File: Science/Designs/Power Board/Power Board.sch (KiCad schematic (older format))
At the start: 13 parts

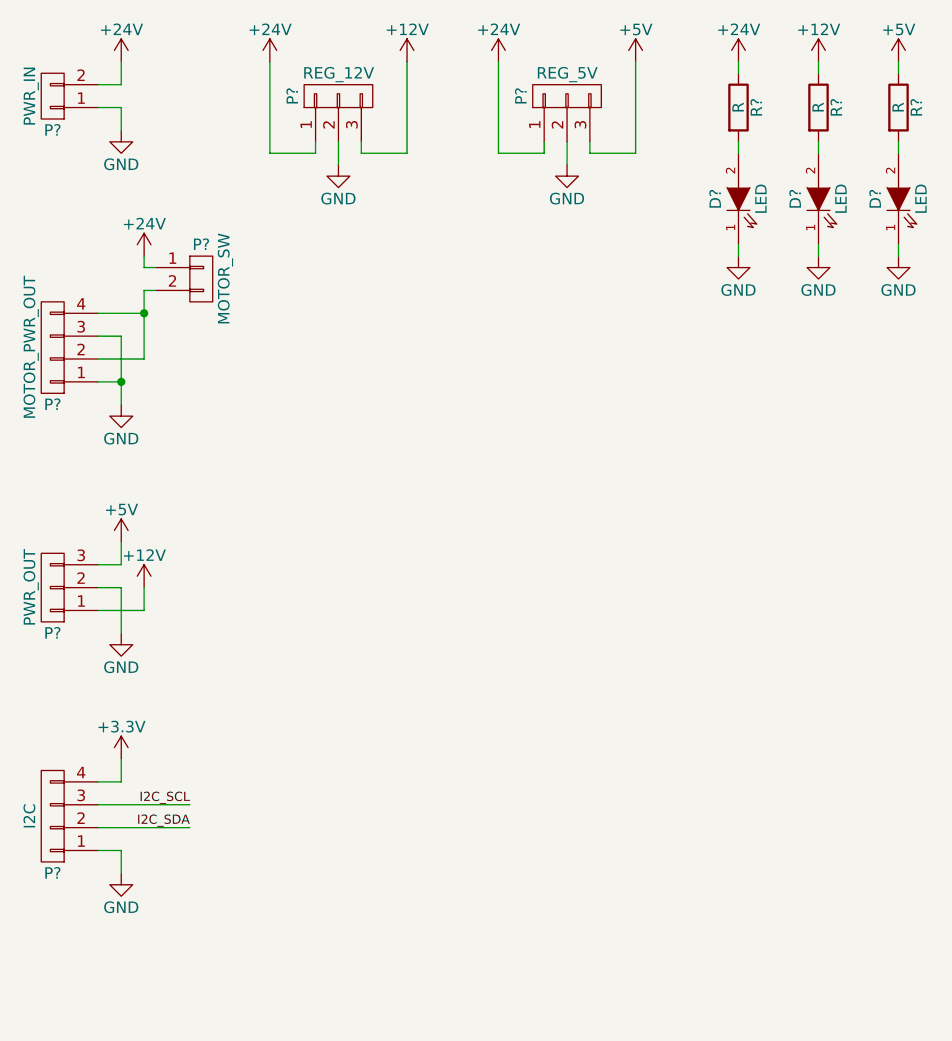
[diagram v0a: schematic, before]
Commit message: Current sensing on power board
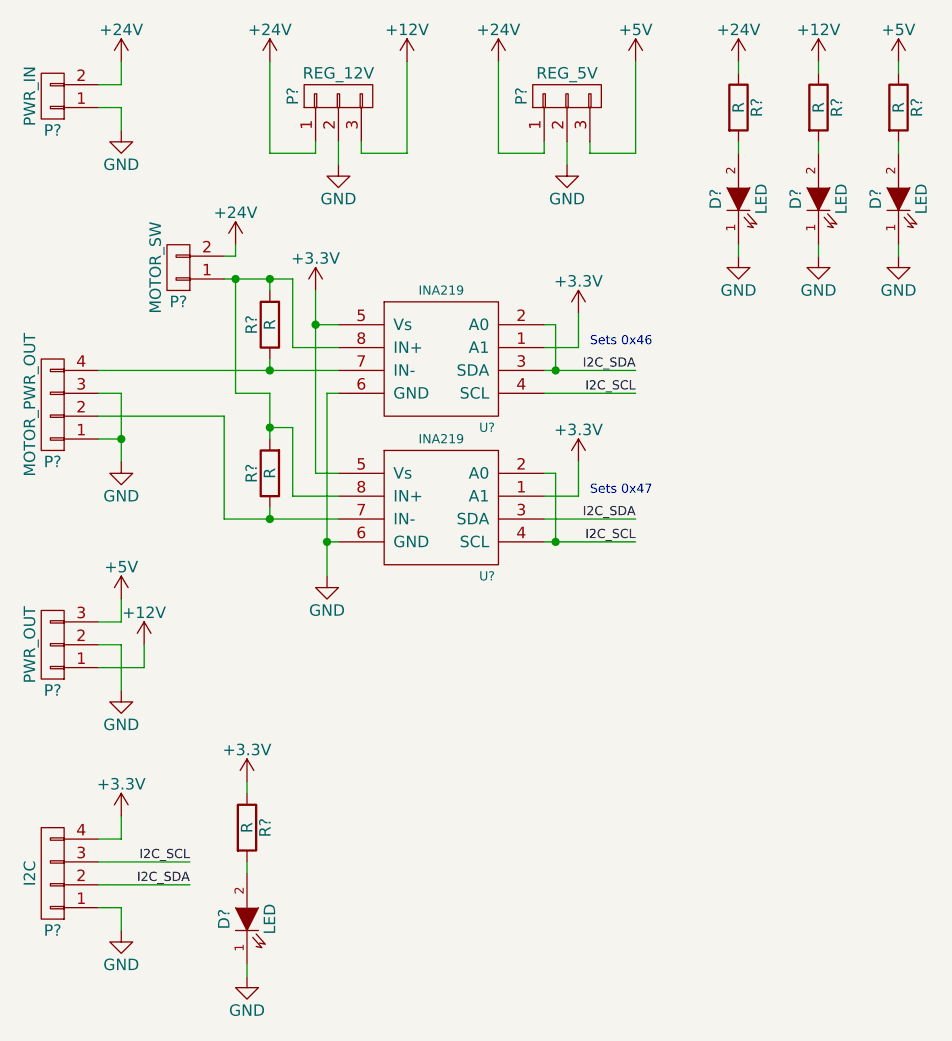
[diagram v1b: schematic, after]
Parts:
- added D?: LED, symbol LED
- added R? (x3): R, symbol R
- added U? (x2): INA219, symbol INA219
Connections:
- net +24V: now also P?.2 (P2); no longer P?.1 (P1)
- net +3V3: now also R?.1, U?.1 (A1), U?.1 (A1), U?.5 (Vs), U?.5 (Vs)
- net +5V: now also R?.1; no longer R?.1
- net GND: now also D?.1 (K), U?.6 (GND), U?.6 (GND)
- net I2C_SCL: now also U?.2 (A0), U?.4 (SCL), U?.4 (SCL)
- net I2C_SDA: now also U?.2 (A0), U?.3 (SDA), U?.3 (SDA)
- new net: P?.2 (P2), R?.1, U?.7 (IN-)
- new net: P?.4 (P4), R?.1, U?.7 (IN-)
- new net: P?.1 (P1), R?.2, R?.2, U?.8 (IN+), U?.8 (IN+)
- new net: D?.2 (A), R?.2
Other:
- note added: "Sets 0x46"
- note added: "Sets 0x47"
- moved on the sheet: D?, P?, R?

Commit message: Adding component values, system current sensor
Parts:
- added C? (x3): 100nF, symbol C
- added R?: 150mΩ, symbol R
- added R?: 2mΩ, symbol R
- added U?: INA219, symbol INA219
- R?: value R -> 1.5kΩ
- R?: value R -> 820Ω
- R?: value R -> 120Ω
- R?: value R -> 2mΩ
- R?: value R -> 10mΩ
- R?: value R -> 220Ω
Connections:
- net +24V: now also R?.1, U?.7 (IN-); no longer P?.2 (P2), P?.2 (P2)
- net +3V3: now also C?.1, C?.1, C?.1, U?.5 (Vs)
- net GND: now also C?.2, C?.2, C?.2, U?.2 (A0), U?.6 (GND)
- net I2C_SCL: now also U?.4 (SCL)
- net I2C_SDA: now also U?.1 (A1), U?.3 (SDA)
- net at P?.4 (P4), R?.1, U?.7 (IN-): now also R?.1
- net at P?.1 (P1), R?.2, R?.2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: now also R?.2
- new net 24V_IN: P?.2 (P2), P?.2 (P2), R?.2, U?.8 (IN+)
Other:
- note added: "Sets 0x48"
- moved on the sheet: P?

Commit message: Fixed issues
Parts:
- removed U? (x3): INA219, symbol INA219
- added U? (x3): INA219, symbol INA219
- P?: value PWR_OUT -> MAIN_PWR_OUT
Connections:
- net +24V: now also U?.7 (IN-)
- net +3V3: now also U?.1 (A1), U?.1 (A1), U?.5 (Vs), U?.5 (Vs), U?.5 (Vs)
- net 24V_IN: now also U?.8 (IN+)
- net GND: now also U?.2 (A0), U?.6 (GND), U?.6 (GND), U?.6 (GND)
- net I2C_SCL: now also U?.2 (A0), U?.4 (SCL), U?.4 (SCL), U?.4 (SCL)
- net I2C_SDA: now also U?.1 (A1), U?.2 (A0), U?.3 (SDA), U?.3 (SDA), U?.3 (SDA)
- net at P?.2 (P2), R?.1: now also U?.7 (IN-)
- net at P?.4 (P4), R?.1, R?.1: now also U?.7 (IN-)
- net at P?.1 (P1), R?.2, R?.2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: now also U?.8 (IN+), U?.8 (IN+)
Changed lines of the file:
@@
 P 1500 3500
 F 0 "P?" H 1500 3700 50  0000 C CNN
-F 1 "PWR_OUT" V 1600 3500 50  0000 C CNN
+F 1 "MAIN_PWR_OUT" V 1600 3500 50  0000 C CNN
 F 2 "" H 1500 3500 50  0000 C CNN
 F 3 "" H 1500 3500 50  0000 C CNN
@@
 	1    1850 1850
 	-1   0    0    1
-$EndComp
-$Comp
-L INA219 U?
-U 1 1 5A23D83B
-P 3200 2250
-F 0 "U?" H 3400 1950 40  0000 C CNN
-F 1 "INA219" H 3200 2550 40  0000 C CNN
-F 2 "" H 3200 2250 40  0001 C CNN
-F 3 "" H 3200 2250 40  0001 C CNN
-	1    3200 2250
-	1    0    0    -1
-$EndComp
-$Comp
-L INA219 U?
-U 1 1 5A23D894
-P 3200 2900
-F 0 "U?" H 3400 2600 40  0000 C CNN
-F 1 "INA219" H 3200 3200 40  0000 C CNN
-F 2 "" H 3200 2900 40  0001 C CNN
-F 3 "" H 3200 2900 40  0001 C CNN
-	1    3200 2900
-	1    0    0    -1
 $EndComp
 $Comp
@@
 Text Notes 3850 2850 0    40   ~ 0
 Sets 0x47
-$Comp
-L INA219 U?
-U 1 1 5A516F51
-P 3700 4000
-F 0 "U?" H 3900 3700 40  0000 C CNN
-F 1 "INA219" H 3700 4300 40  0000 C CNN
-F 2 "" H 3700 4000 40  0001 C CNN
-F 3 "" H 3700 4000 40  0001 C CNN
-	1    3700 4000
-	1    0    0    -1
-$EndComp
 Text Label 4550 4050 2    40   ~ 0
 I2C_SDA
@@
 	2250 2250 2250 2300
 Connection ~ 2250 2300
+$Comp
+L INA219 U?
+U 1 1 5A5E4452
+P 3200 2250
+F 0 "U?" H 3400 1950 40  0000 C CNN
+F 1 "INA219" H 3200 2550 40  0000 C CNN
+F 2 "" H 3200 2250 40  0001 C CNN
+F 3 "" H 3200 2250 40  0001 C CNN
+	1    3200 2250
+	1    0    0    -1
+$EndComp
+$Comp
+L INA219 U?
+U 1 1 5A5E4536
+P 3200 2900
+F 0 "U?" H 3400 2600 40  0000 C CNN
+F 1 "INA219" H 3200 3200 40  0000 C CNN
+F 2 "" H 3200 2900 40  0001 C CNN
+F 3 "" H 3200 2900 40  0001 C CNN
+	1    3200 2900
+	1    0    0    -1
+$EndComp
+$Comp
+L INA219 U?
+U 1 1 5A5E4596
+P 3700 4000
+F 0 "U?" H 3900 3700 40  0000 C CNN
+F 1 "INA219" H 3700 4300 40  0000 C CNN
+F 2 "" H 3700 4000 40  0001 C CNN
+F 3 "" H 3700 4000 40  0001 C CNN
+	1    3700 4000
+	1    0    0    -1
+$EndComp
 $EndSCHEMATC

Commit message: Began Power Board layout
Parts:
- D? (x4): symbol LED -> LED-RESCUE-Power_Board
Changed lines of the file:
@@
 EESchema Schematic File Version 2
+LIBS:Power Board-rescue
 LIBS:power
 LIBS:device
@@
 $EndComp
 Wire Wire Line
-	1700 2300 2250 2300
-Wire Wire Line
-	2250 2300 2450 2300
-Wire Wire Line
-	2450 2300 2750 2300
+	1700 2300 2750 2300
 Wire Wire Line
 	1700 2500 2250 2500
@@
 	1700 2400 1800 2400
 Wire Wire Line
-	1800 2400 1800 2600
-Wire Wire Line
-	1800 2600 1800 2700
+	1800 2400 1800 2700
 Wire Wire Line
 	1700 2600 1800 2600
@@
 $EndComp
 $Comp
-L LED D?
+L LED-RESCUE-Power_Board D?
 U 1 1 5A235063
 P 4500 1550
@@
 $EndComp
 $Comp
-L LED D?
+L LED-RESCUE-Power_Board D?
 U 1 1 5A235495
 P 4850 1550
@@
 $EndComp
 $Comp
-L LED D?
+L LED-RESCUE-Power_Board D?
 U 1 1 5A235672
 P 2350 4700
@@
 Connection ~ 2450 2300
 Wire Wire Line
-	2250 2950 2450 2950
-Wire Wire Line
-	2450 2950 2750 2950
+	2250 2950 2750 2950
 Wire Wire Line
 	2450 2950 2450 2900
@@
 Connection ~ 2450 2950
 Wire Wire Line
-	2450 2400 2450 2550
-Wire Wire Line
-	2450 2550 2450 2600
+	2450 2400 2450 2600
 Wire Wire Line
 	2450 2550 2550 2550
@@
 Connection ~ 2100 1900
 Wire Wire Line
-	2050 1900 2100 1900
-Wire Wire Line
-	2100 1900 2250 1900
-Wire Wire Line
-	2250 1900 2450 1900
-Wire Wire Line
-	2450 1900 2550 1900
+	2050 1900 2550 1900
 Wire Wire Line
 	2050 1800 2350 1800
 Wire Wire Line
-	2650 1950 2650 2100
-Wire Wire Line
-	2650 2100 2650 2750
+	2650 1950 2650 2750
 Connection ~ 2650 2100
 Wire Wire Line
 	2750 2400 2700 2400
 Wire Wire Line
-	2700 2400 2700 3050
-Wire Wire Line
-	2700 3050 2700 3200
+	2700 2400 2700 3200
 Wire Wire Line
 	2700 3050 2750 3050
@@
 I2C_SCL
 Wire Wire Line
-	3650 3050 3700 3050
-Wire Wire Line
-	3700 3050 4050 3050
+	3650 3050 4050 3050
 Wire Wire Line
 	3650 2950 4050 2950
@@
 	3650 2400 4050 2400
 Wire Wire Line
-	3650 2300 3700 2300
-Wire Wire Line
-	3700 2300 4050 2300
+	3650 2300 4050 2300
 $Comp
 L +3.3V #PWR?
@@
 $EndComp
 $Comp
-L LED D?
+L LED-RESCUE-Power_Board D?
 U 1 1 5A2432EE
 P 5200 1550
@@
 P 3000 3850
 F 0 "R?" V 3080 3850 50  0000 C CNN
-F 1 "150mΩ" V 3000 3850 50  0000 C CNN
+F 1 "150mΩ" V 3000 3850 39  0000 C CNN
 F 2 "" V 2930 3850 50  0000 C CNN
 F 3 "" H 3000 3850 50  0000 C CNN
@@
 	3250 3950 3100 3950
 Wire Wire Line
-	3100 3950 3100 3650
+	3100 3650 3100 3950
 Wire Wire Line
 	3000 3700 3000 3700
 Wire Wire Line
-	3100 3650 3000 3650
-Wire Wire Line
-	3000 3650 2750 3650
+	2750 3650 3100 3650
 Wire Wire Line
 	3000 3650 3000 3700
 Wire Wire Line
-	2750 4050 3000 4050
-Wire Wire Line
-	3000 4050 3250 4050
+	2750 4050 3250 4050
 Wire Wire Line
 	3000 4050 3000 4000
@@
 	4150 4150 4550 4150
 Wire Wire Line
-	4150 4050 4200 4050
-Wire Wire Line
-	4200 4050 4550 4050
+	4150 4050 4550 4050
 Wire Wire Line
 	4200 3850 4200 3650
